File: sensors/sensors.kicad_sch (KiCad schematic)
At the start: 10 parts

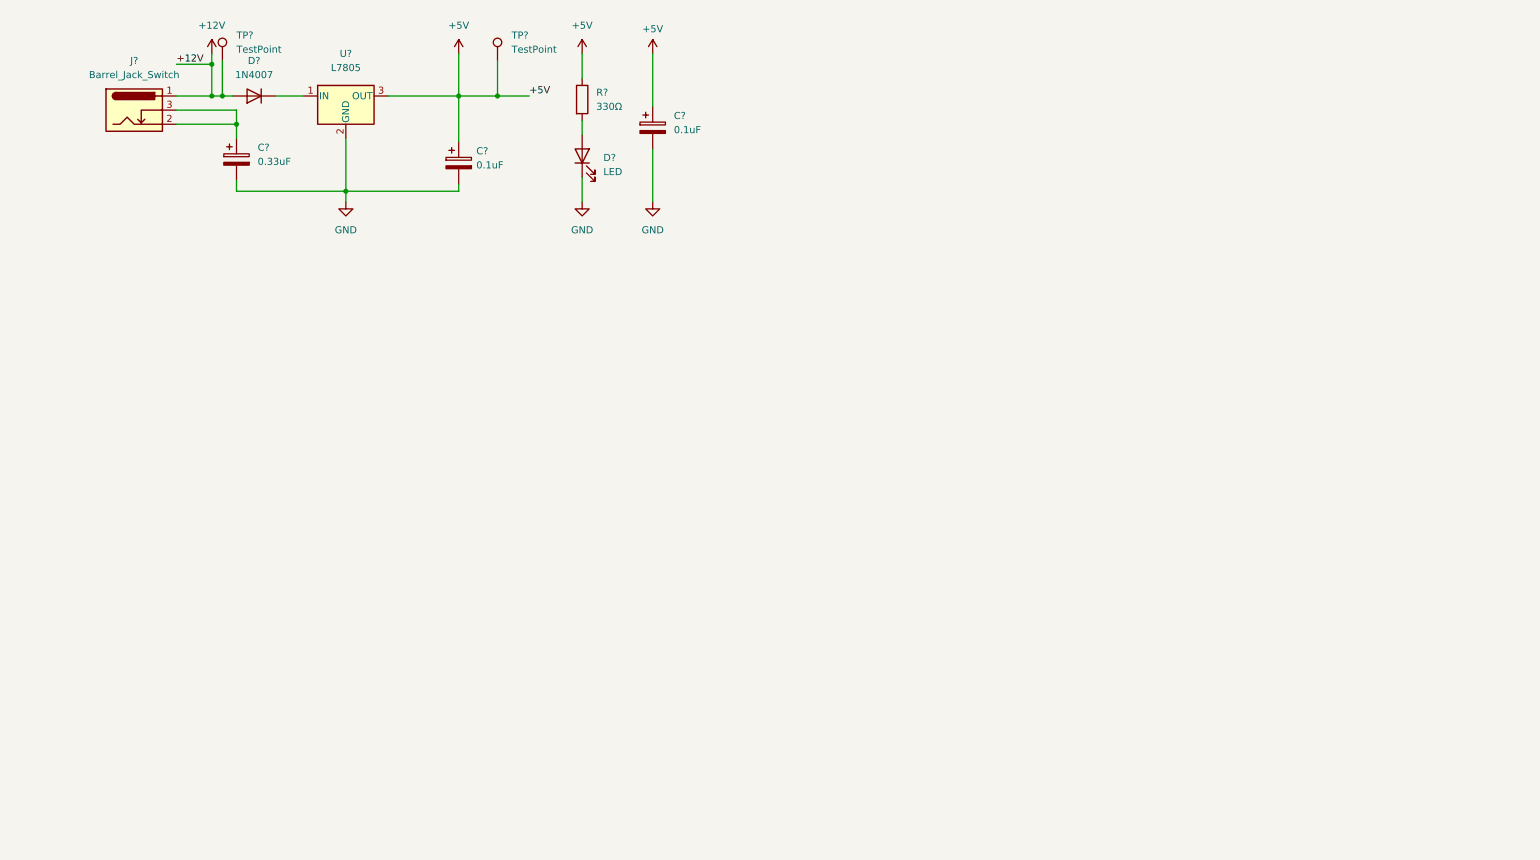
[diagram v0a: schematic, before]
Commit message: Version 2022.09.19 - Added Raspberry Pi & Mega
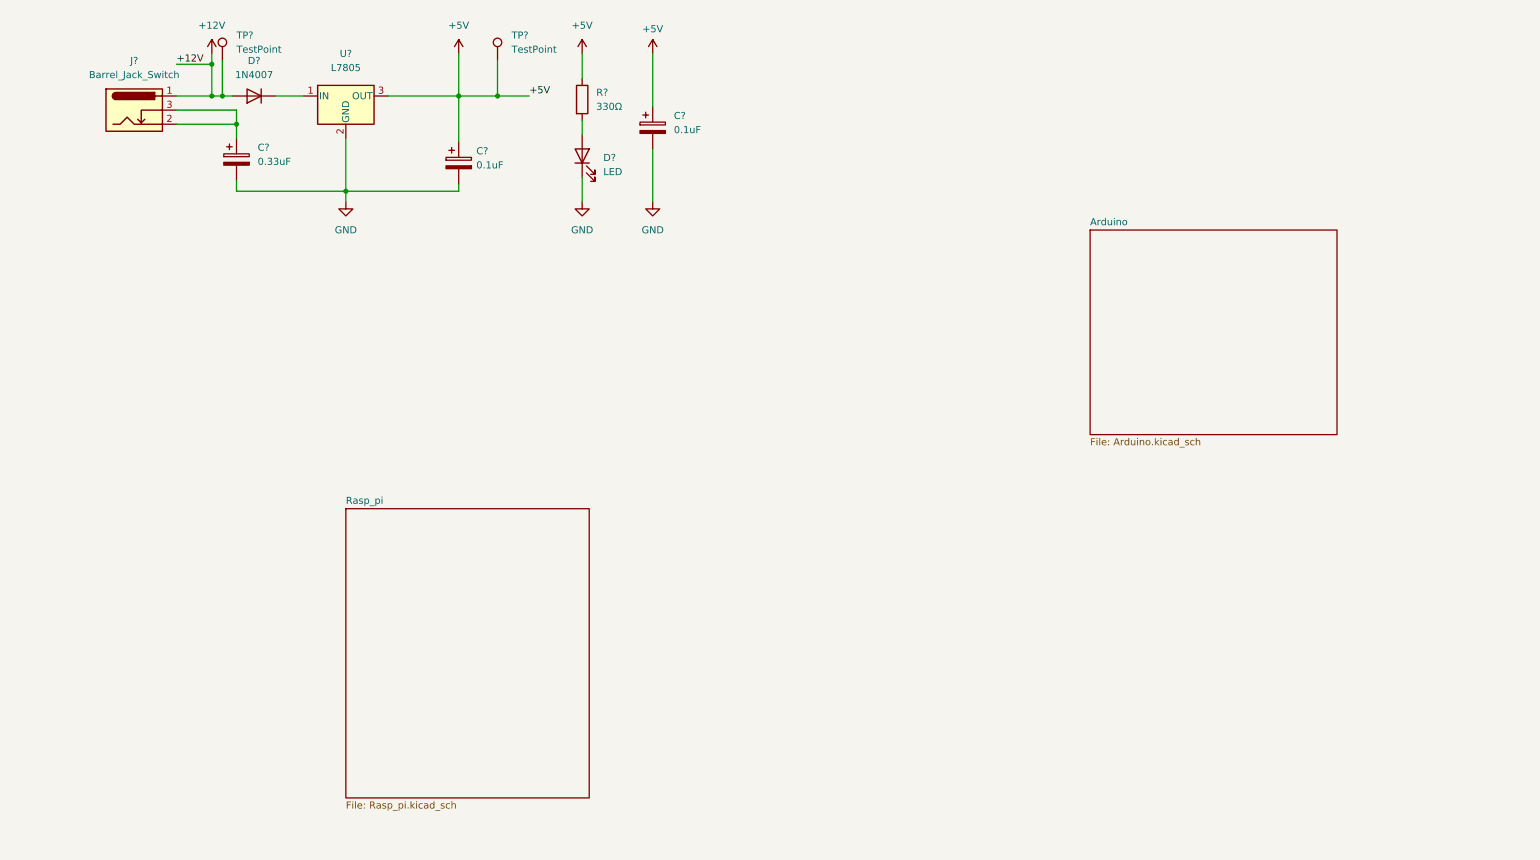
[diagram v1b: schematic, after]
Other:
- added sheet Arduino (Arduino.kicad_sch)
- added sheet Rasp_pi (Rasp_pi.kicad_sch)
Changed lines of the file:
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@@
     (pin "3")
+  )
+  (sheet (at 71.755 107.95) (size 43.815 52.07) (fields_autoplaced)
+    (stroke (width 0.1524) (type solid) (color 0 0 0 0))
+    (fill (color 0 0 0 0.0000))
+    (property "Sheet name" "Rasp_pi" (id 0) (at 71.755 107.2384 0)
+      (effects (font (size 1.27 1.27)) (justify left bottom))
+    )
+    (property "Sheet file" "Rasp_pi.kicad_sch" (id 1) (at 71.755 160.6046 0)
+      (effects (font (size 1.27 1.27)) (justify left top))
+    )
+  )
+  (sheet (at 205.74 57.785) (size 44.45 36.83) (fields_autoplaced)
+    (stroke (width 0.1524) (type solid) (color 0 0 0 0))
+    (fill (color 0 0 0 0.0000))
+    (property "Sheet name" "Arduino" (id 0) (at 205.74 57.0734 0)
+      (effects (font (size 1.27 1.27)) (justify left bottom))
+    )
+    (property "Sheet file" "Arduino.kicad_sch" (id 1) (at 205.74 95.1996 0)
+      (effects (font (size 1.27 1.27)) (justify left top))
+    )
   )
   (sheet_instances
     (path "/" (page "1"))
+    (path "/d22c6e0e-8d6d-4131-8956-db92227f13bc" (page "2"))
+    (path "/37e107f4-8cbf-453d-a226-e8f63571ca96" (page "3"))
   )
   (symbol_instances
@@
       (reference "D?") (unit 1) (value "1N4007") (footprint "Diode_THT:D_DO-41_SOD81_P10.16mm_Horizontal")
     )
+    (path "/37e107f4-8cbf-453d-a226-e8f63571ca96/dfaeec22-2638-4fb5-bf95-905695ea8b23"
+      (reference "J?") (unit 1) (value "Raspberry_Pi_2_3") (footprint "Connector_PinHeader_2.54mm:PinHeader_2x20_P2.54mm_Vertical")
+    )
     (path "/eb4d7b06-f329-4c44-9bca-d22a891e35c2"
       (reference "J?") (unit 1) (value "Barrel_Jack_Switch") (footprint "Connector_BarrelJack:BarrelJack_Horizontal")
@@
       (reference "U?") (unit 1) (value "L7805") (footprint "Package_TO_SOT_THT:TO-220-3_Vertical")
     )
+    (path "/d22c6e0e-8d6d-4131-8956-db92227f13bc/9e0a981b-05b3-467f-8476-12c979e50544"
+      (reference "XA?") (unit 1) (value "Arduino_Mega2560_Shield") (footprint "Arduino:Arduino_Mega2560_Shield")
+    )
   )

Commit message: Version 2022.09.20 - Added Terminal Blocks
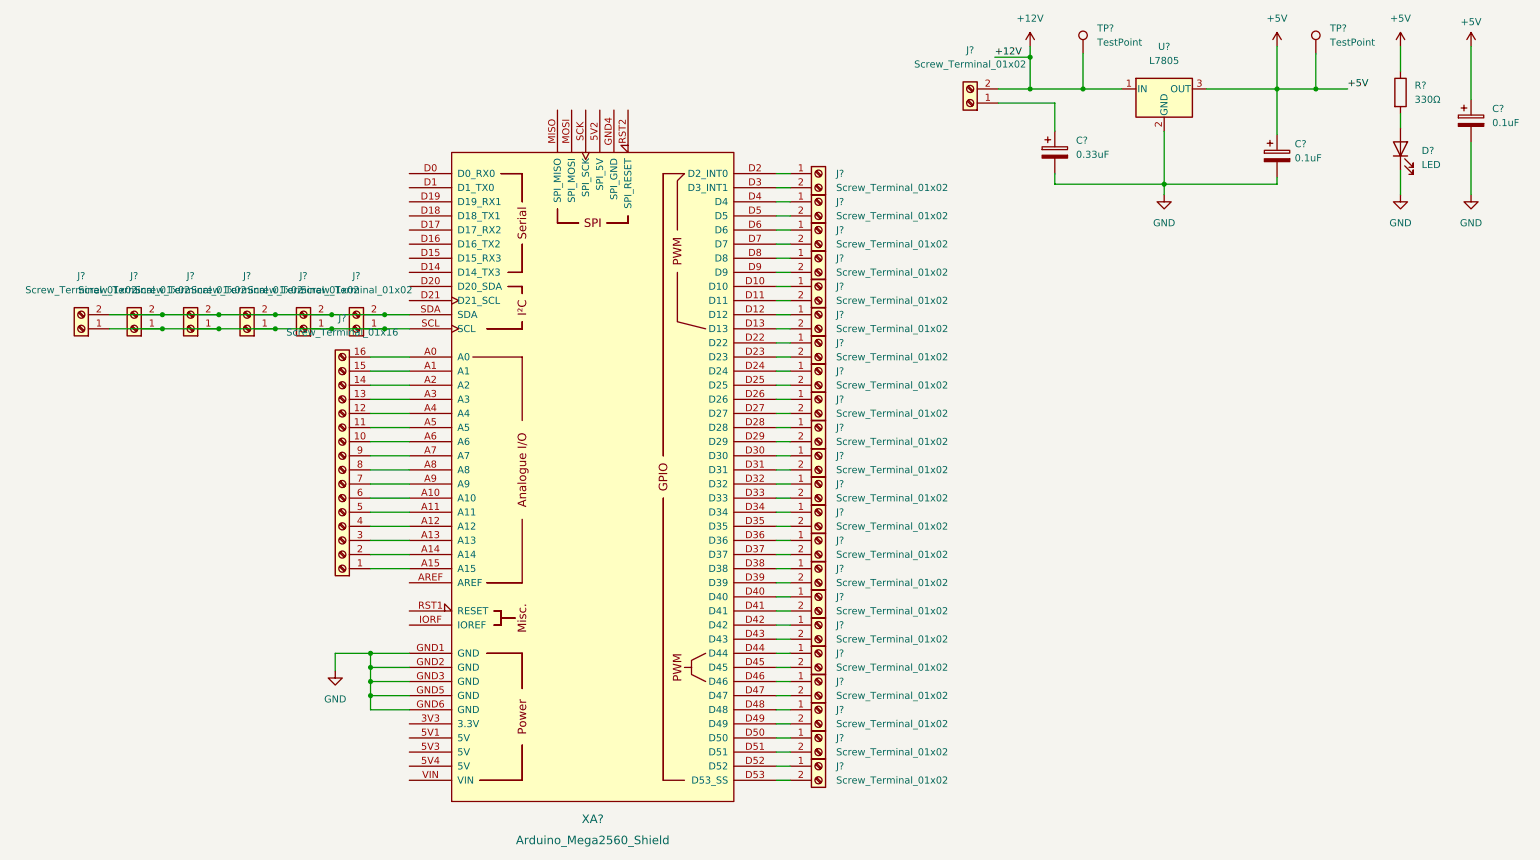
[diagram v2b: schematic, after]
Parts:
- removed D?: 1N4007, Diode_THT:D_DO-41_SOD81_P10.16mm_Horizontal, symbol Diode:1N4007
- removed J?: Barrel_Jack_Switch, Connector_BarrelJack:BarrelJack_Horizontal, symbol Connector:Barrel_Jack_Switch
- added J? (x29): Screw_Terminal_01x02, symbol Connector:Screw_Terminal_01x02
- added J?: Screw_Terminal_01x16, symbol Connector:Screw_Terminal_01x16
- added XA?: Arduino_Mega2560_Shield, Arduino:Arduino_Mega2560_Shield, symbol arduino:Arduino_Mega2560_Shield
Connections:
- net +12V: now also U?.1 (IN), J?.2 (Pin_2)
- net GND: now also XA?.GND1 (GND), XA?.GND2 (GND), XA?.GND3 (GND), XA?.GND5 (GND), XA?.GND6 (GND)
- net at C?.1: now also J?.1 (Pin_1)
- new net: J?.1 (Pin_1), XA?.D34
- new net: J?.2 (Pin_2), XA?.D35
- new net: J?.1 (Pin_1), XA?.D2 (D2_INT0)
- new net: J?.2 (Pin_2), XA?.D3 (D3_INT1)
- new net: J?.1 (Pin_1), XA?.D24
- new net: J?.2 (Pin_2), XA?.D25
- new net: J?.1 (Pin_1), XA?.D28
- new net: J?.2 (Pin_2), XA?.D29
- new net: J?.1 (Pin_1), XA?.D4
- new net: J?.2 (Pin_2), XA?.D5
- new net: J?.1 (Pin_1), XA?.D26
- new net: J?.2 (Pin_2), XA?.D27
- new net: J?.1 (Pin_1), XA?.D30
- new net: J?.2 (Pin_2), XA?.D31
- new net: J?.16 (Pin_16), XA?.A0
- new net: J?.15 (Pin_15), XA?.A1
- new net: J?.6 (Pin_6), XA?.A10
- new net: J?.5 (Pin_5), XA?.A11
- new net: J?.4 (Pin_4), XA?.A12
- new net: J?.3 (Pin_3), XA?.A13
- new net: J?.2 (Pin_2), XA?.A14
- new net: J?.1 (Pin_1), XA?.A15
- new net: J?.14 (Pin_14), XA?.A2
- new net: J?.13 (Pin_13), XA?.A3
- new net: J?.12 (Pin_12), XA?.A4
- new net: J?.11 (Pin_11), XA?.A5
- new net: J?.10 (Pin_10), XA?.A6
- new net: J?.9 (Pin_9), XA?.A7
- new net: J?.8 (Pin_8), XA?.A8
- new net: J?.7 (Pin_7), XA?.A9
- new net: J?.1 (Pin_1), XA?.D10
- new net: J?.2 (Pin_2), XA?.D11
- new net: J?.1 (Pin_1), XA?.D12
- new net: J?.2 (Pin_2), XA?.D13
- new net: J?.1 (Pin_1), XA?.D22
- new net: J?.2 (Pin_2), XA?.D23
- new net: J?.1 (Pin_1), XA?.D32
- new net: J?.2 (Pin_2), XA?.D33
- new net: J?.1 (Pin_1), XA?.D36
- new net: J?.2 (Pin_2), XA?.D37
- new net: J?.1 (Pin_1), XA?.D38
- new net: J?.2 (Pin_2), XA?.D39
- new net: J?.1 (Pin_1), XA?.D40
- new net: J?.2 (Pin_2), XA?.D41
- new net: J?.1 (Pin_1), XA?.D42
- new net: J?.2 (Pin_2), XA?.D43
- new net: J?.1 (Pin_1), XA?.D44
- new net: J?.2 (Pin_2), XA?.D45
- new net: J?.1 (Pin_1), XA?.D46
- new net: J?.2 (Pin_2), XA?.D47
- new net: J?.1 (Pin_1), XA?.D48
- new net: J?.2 (Pin_2), XA?.D49
- new net: J?.1 (Pin_1), XA?.D50
- new net: J?.2 (Pin_2), XA?.D51
- new net: J?.1 (Pin_1), XA?.D52
- new net: J?.2 (Pin_2), XA?.D53 (D53_SS)
- new net: J?.1 (Pin_1), XA?.D6
- new net: J?.2 (Pin_2), XA?.D7
- new net: J?.1 (Pin_1), XA?.D8
- new net: J?.2 (Pin_2), XA?.D9
- new net: J?.1 (Pin_1), J?.1 (Pin_1), J?.1 (Pin_1), J?.1 (Pin_1), J?.1 (Pin_1), J?.1 (Pin_1), XA?.SCL
- new net: J?.2 (Pin_2), J?.2 (Pin_2), J?.2 (Pin_2), J?.2 (Pin_2), J?.2 (Pin_2), J?.2 (Pin_2), XA?.SDA
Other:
- removed sheet Arduino
- removed sheet Rasp_pi
- moved on the sheet: C?, D?, R?, TP?, U?
